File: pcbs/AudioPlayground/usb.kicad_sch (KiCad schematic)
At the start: 19 parts, among them J3 USB_C_Receptacle_USB2.0_14P, U3 USB2422/MJ, Y3 24MHz

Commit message: Add LCSC and fix RF
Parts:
- removed D4: PRTR5V0U2X, Package_TO_SOT_SMD:SOT-143, symbol Power_Protection:PRTR5V0U2X
- added U15: USBLC6-2P6, Package_TO_SOT_SMD:SOT-666, symbol Power_Protection:USBLC6-2P6
- C2, C48: LCSC (none) -> C1525
- C25: value 0.1uF -> 100nF; LCSC (none) -> C1525
- C35, C47, C49: LCSC (none) -> C52923
- C36, C46: LCSC (none) -> C1549
- J3: LCSC (none) -> C2765186
- R12: LCSC (none) -> C25752
- R15, R16, R17: LCSC (none) -> C25794
- R19, R2: LCSC (none) -> C25905
- R6: LCSC (none) -> C25744
- U3: LCSC (none) -> C622611
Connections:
- net D+: now also U15.3 (I/O2); no longer U3.20 (USBDP_UP)
- net D-: now also U15.1 (I/O1); no longer U3.19 (USBDM_UP)
- net GND: now also U15.2 (GND)
- net VBUS: now also U15.5 (VBUS)
- new net ESD_D+: U15.4 (I/O2), U3.20 (USBDP_UP)
- new net ESD_D-: U15.6 (I/O1), U3.19 (USBDM_UP)

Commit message: Update MICs
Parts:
- Y3: LCSC (none) -> C41383244
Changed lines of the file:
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@@
+			)
+		)
+		(property "LCSC" "C41383244"
+			(at 146.05 130.81 0)
+			(effects
+				(font
+					(size 1.27 1.27)
+				)
+				(hide yes)
 			)
 		)

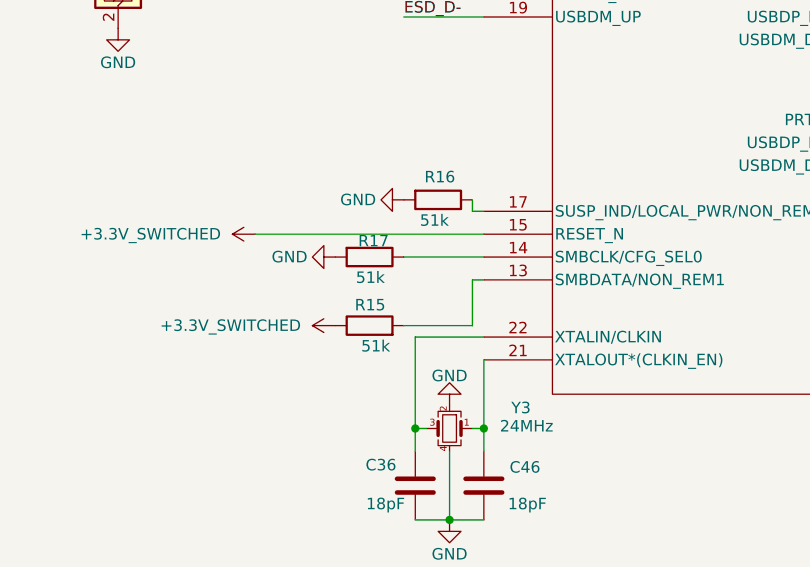
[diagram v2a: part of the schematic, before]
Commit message: Fix USB Pullups
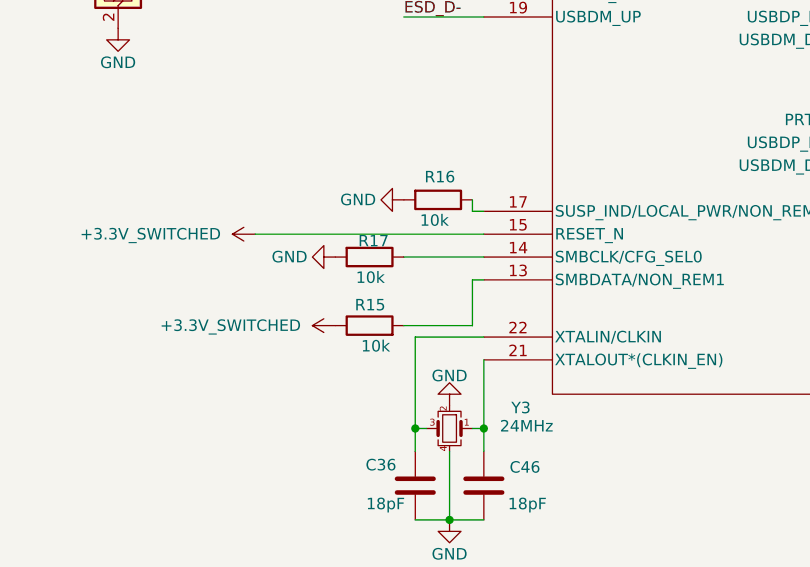
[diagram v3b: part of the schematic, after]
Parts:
- R15, R16, R17: value 51k -> 10k; LCSC C25794 -> C25744
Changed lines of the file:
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@@
 			)
 		)
-		(property "Value" "51k"
+		(property "Value" "10k"
 			(at 142.748 107.696 90)
 			(effects
@@
 			)
 		)
-		(property "LCSC" "C25794"
+		(property "LCSC" "C25744"
 			(at 144.78 105.41 90)
 			(effects
@@
 			)
 		)
-		(property "Value" "51k"
+		(property "Value" "10k"
 			(at 135.636 114.046 90)
 			(effects
@@
 			)
 		)
-		(property "LCSC" "C25794"
+		(property "LCSC" "C25744"
 			(at 137.16 111.76 90)
 			(effects
@@
 			)
 		)
-		(property "Value" "51k"
+		(property "Value" "10k"
 			(at 139.446 121.666 90)
 			(effects
@@
 			)
 		)
-		(property "LCSC" "C25794"
+		(property "LCSC" "C25744"
 			(at 137.16 119.38 90)
 			(effects

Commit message: Improve Optic
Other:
- title: (none) -> LE Audio Playground
- moved on the sheet: C2, C25, C35, C36, C46, C47, C48, C49, J3, R12, R15, R16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
